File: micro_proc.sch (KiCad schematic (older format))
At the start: 1 part

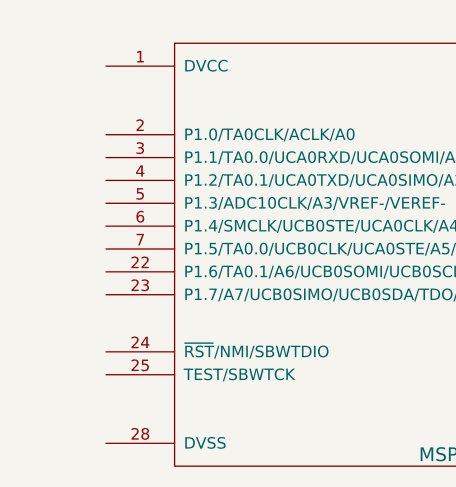
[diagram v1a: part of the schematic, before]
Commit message: added headlight sheet, led, dac
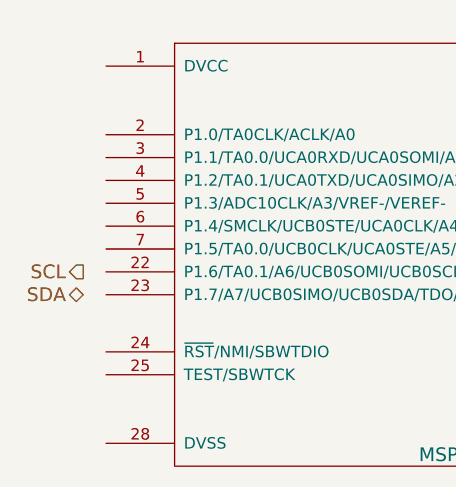
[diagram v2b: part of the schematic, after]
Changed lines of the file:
@@
 $Descr A4 11693 8268
 encoding utf-8
-Sheet 7 16
+Sheet 7 17
 Title ""
-Date "6 dec 2013"
+Date "7 dec 2013"
 Rev ""
 Comp ""
@@
 	1    0    0    -1
 $EndComp
+Text HLabel 4100 2950 0    60   BiDi ~ 0
+SDA
+Text HLabel 4100 2850 0    60   Output ~ 0
+SCL
 $EndSCHEMATC

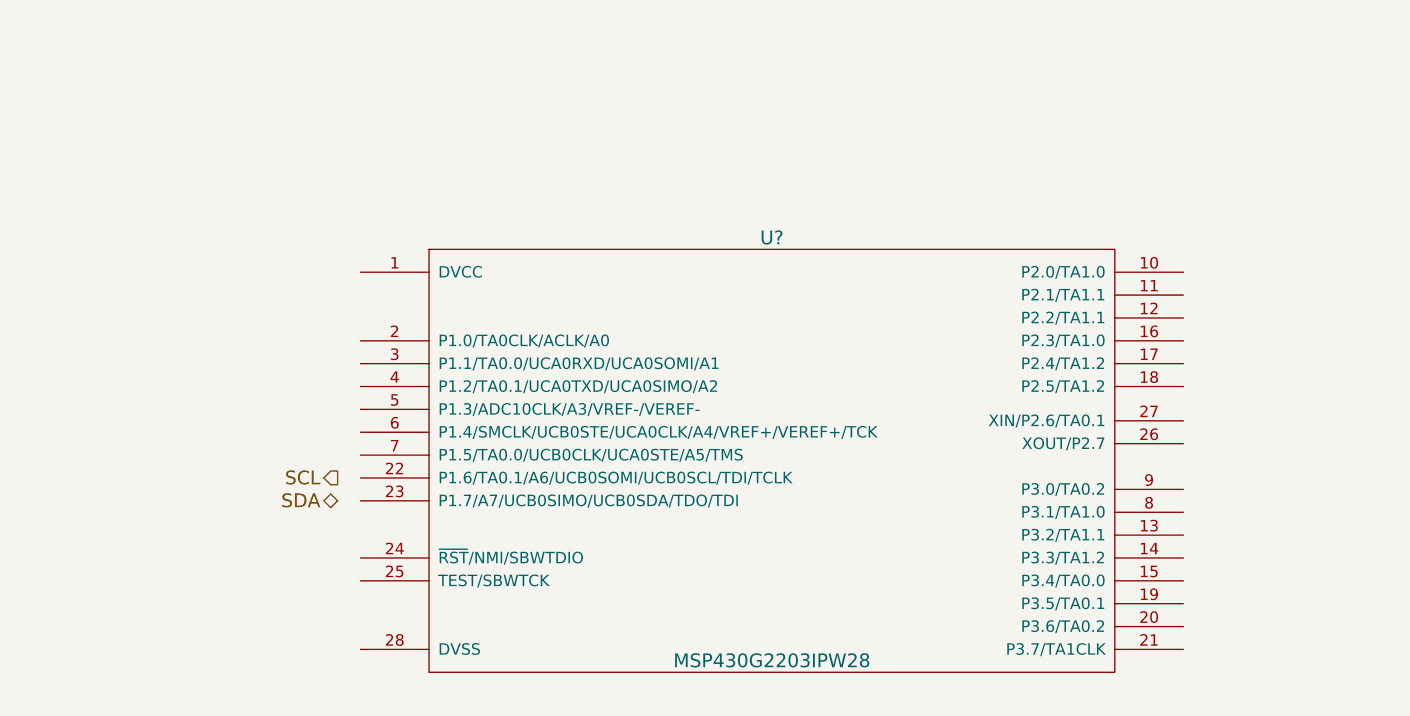
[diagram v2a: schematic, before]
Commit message: organized proc sheet I/O, organized I2C bus structure
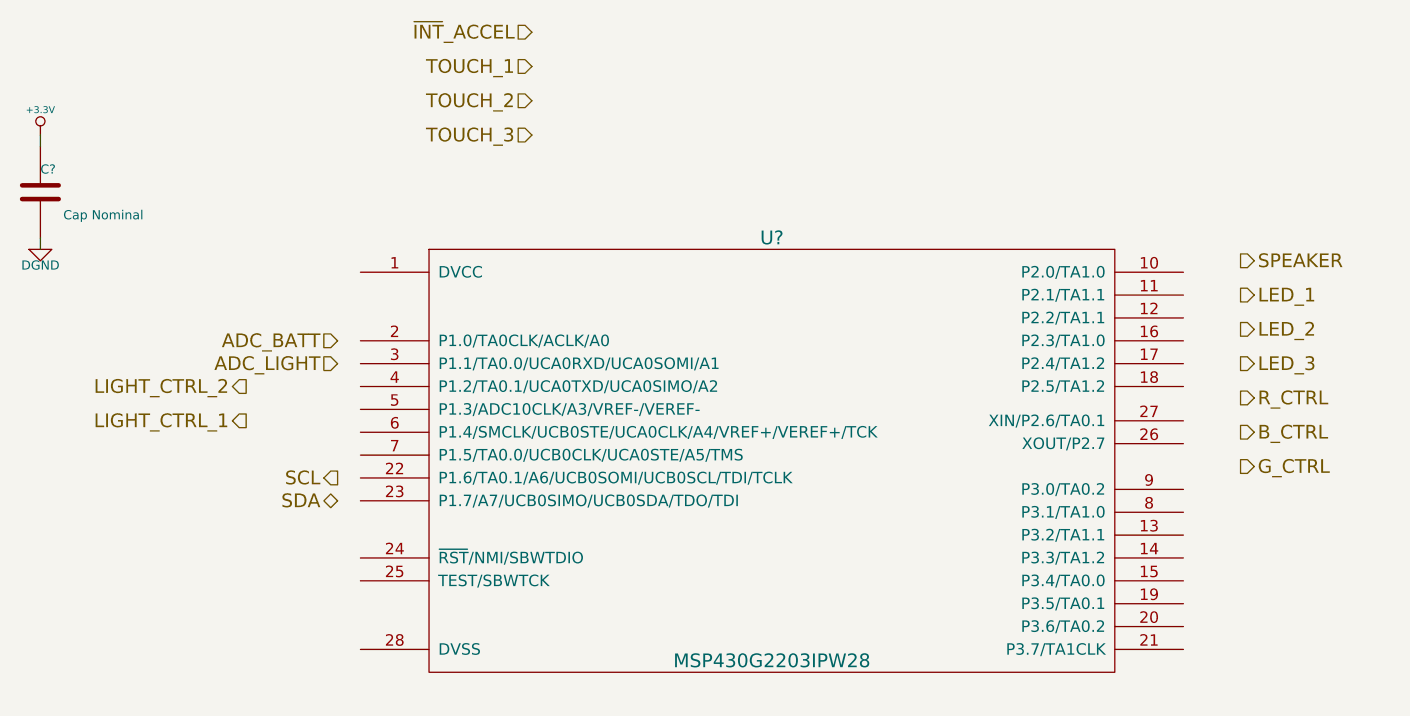
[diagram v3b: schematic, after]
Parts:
- added C?: Cap Nominal, ~, symbol C
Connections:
- new net +3.3V: C?.1
- new net DGND: C?.2
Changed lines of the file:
@@
 Text HLabel 4100 2850 0    60   Output ~ 0
 SCL
+$Comp
+L C C?
+U 1 1 52A38C98
+P 2800 1600
+F 0 "C?" H 2800 1700 40  0000 L CNN
+F 1 "Cap Nominal" H 2900 1500 40  0000 L CNN
+F 2 "~" H 2838 1450 30  0000 C CNN
+F 3 "~" H 2800 1600 60  0000 C CNN
+	1    2800 1600
+	1    0    0    -1
+$EndComp
+$Comp
+L +3.3V #PWR?
+U 1 1 52A38C9E
+P 2800 1350
+F 0 "#PWR?" H 2800 1310 30  0001 C CNN
+F 1 "+3.3V" H 2800 1460 30  0000 C CNN
+F 2 "" H 2800 1350 60  0000 C CNN
+F 3 "" H 2800 1350 60  0000 C CNN
+	1    2800 1350
+	1    0    0    -1
+$EndComp
+$Comp
+L DGND #PWR?
+U 1 1 52A38CA4
+P 2800 1850
+F 0 "#PWR?" H 2800 1850 40  0001 C CNN
+F 1 "DGND" H 2800 1780 40  0000 C CNN
+F 2 "" H 2800 1850 60  0000 C CNN
+F 3 "" H 2800 1850 60  0000 C CNN
+	1    2800 1850
+	1    0    0    -1
+$EndComp
+Wire Wire Line
+	2800 1350 2800 1400
+Wire Wire Line
+	2800 1800 2800 1850
+Text HLabel 4100 2250 0    60   Input ~ 0
+ADC_BATT
+Text HLabel 4100 2350 0    60   Input ~ 0
+ADC_LIGHT
+Text HLabel 4950 900  0    60   Input ~ 0
+~INT~_ACCEL
+Text HLabel 4950 1050 0    60   Input ~ 0
+TOUCH_1
+Text HLabel 4950 1200 0    60   Input ~ 0
+TOUCH_2
+Text HLabel 4950 1350 0    60   Input ~ 0
+TOUCH_3
+Text HLabel 8050 1900 2    60   Output ~ 0
+SPEAKER
+Text HLabel 8050 2050 2    60   Output ~ 0
+LED_1
+Text HLabel 8050 2200 2    60   Output ~ 0
+LED_2
+Text HLabel 8050 2350 2    60   Output ~ 0
+LED_3
+Text HLabel 8050 2500 2    60   Output ~ 0
+R_CTRL
+Text HLabel 8050 2650 2    60   Output ~ 0
+B_CTRL
+Text HLabel 8050 2800 2    60   Output ~ 0
+G_CTRL
+Text HLabel 3700 2600 0    60   Output ~ 0
+LIGHT_CTRL_1
+Text HLabel 3700 2450 0    60   Output ~ 0
+LIGHT_CTRL_2
 $EndSCHEMATC

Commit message: continued fleshing out proc
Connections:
- net +3.3V: now also U?.1 (DVCC)
- net ADC_BATT: now also U?.2 (P1.0/TA0CLK/ACLK/A0)
- net ADC_LIGHT: now also U?.5 (P1.3/ADC10CLK/A3/VREF-/VEREF-)
- net B_CTRL: now also U?.20 (P3.6/TA0.2)
- net DGND: now also U?.28 (DVSS)
- net G_CTRL: now also U?.19 (P3.5/TA0.1)
- net LED_1: now also U?.8 (P3.1/TA1.0)
- net LED_2: now also U?.13 (P3.2/TA1.1)
- net LED_3: now also U?.14 (P3.3/TA1.2)
- net LIGHT_CTRL_1: now also U?.27 (XIN/P2.6/TA0.1)
- net LIGHT_CTRL_2: now also U?.26 (XOUT/P2.7)
- net R_CTRL: now also U?.15 (P3.4/TA0.0)
- net SCL: now also U?.22 (P1.6/TA0.1/A6/UCB0SOMI/UCB0SCL/TDI/TCLK)
- net SDA: now also U?.23 (P1.7/A7/UCB0SIMO/UCB0SDA/TDO/TDI)
- net SPEAKER: now also U?.9 (P3.0/TA0.2)
- net TOUCH_1: now also U?.11 (P2.1/TA1.1)
- net TOUCH_2: now also U?.12 (P2.2/TA1.1)
- net TOUCH_3: now also U?.16 (P2.3/TA1.0)
- net ~INT~_ACCEL: now also U?.10 (P2.0/TA1.0)
- net UART_RX: now reaches U?.3 (P1.1/TA0.0/UCA0RXD/UCA0SOMI/A1)
- net UART_TX: now reaches U?.4 (P1.2/TA0.1/UCA0TXD/UCA0SIMO/A2)
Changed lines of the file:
@@
 Sheet 7 17
 Title ""
-Date "7 dec 2013"
+Date "8 dec 2013"
 Rev ""
 Comp ""
@@
 Text HLabel 4100 2250 0    60   Input ~ 0
 ADC_BATT
+Text HLabel 4100 2550 0    60   Input ~ 0
+ADC_LIGHT
+Text HLabel 7900 1950 2    60   Input ~ 0
+~INT~_ACCEL
+Text HLabel 7900 2050 2    60   Input ~ 0
+TOUCH_1
+Text HLabel 7900 2150 2    60   Input ~ 0
+TOUCH_2
+Text HLabel 7900 2250 2    60   Input ~ 0
+TOUCH_3
+Text HLabel 7900 2900 2    60   Output ~ 0
+SPEAKER
+Text HLabel 7900 3000 2    60   Output ~ 0
+LED_1
+Text HLabel 7900 3100 2    60   Output ~ 0
+LED_2
+Text HLabel 7900 3200 2    60   Output ~ 0
+LED_3
+Text HLabel 7900 3300 2    60   Output ~ 0
+R_CTRL
+Text HLabel 7900 3500 2    60   Output ~ 0
+B_CTRL
+Text HLabel 7900 3400 2    60   Output ~ 0
+G_CTRL
+Text HLabel 7900 2600 2    60   Output ~ 0
+LIGHT_CTRL_1
+Text HLabel 7900 2700 2    60   Output ~ 0
+LIGHT_CTRL_2
+Wire Wire Line
+	4100 2950 4200 2950
+Wire Wire Line
+	4100 2850 4200 2850
+$Comp
+L +3.3V #PWR?
+U 1 1 52A4573A
+P 4200 1850
+F 0 "#PWR?" H 4200 1810 30  0001 C CNN
+F 1 "+3.3V" H 4200 1960 30  0000 C CNN
+F 2 "" H 4200 1850 60  0000 C CNN
+F 3 "" H 4200 1850 60  0000 C CNN
+	1    4200 1850
+	1    0    0    -1
+$EndComp
+Wire Wire Line
+	4200 1850 4200 1950
+$Comp
+L DGND #PWR?
+U 1 1 52A45745
+P 4200 3700
+F 0 "#PWR?" H 4200 3700 40  0001 C CNN
+F 1 "DGND" H 4200 3630 40  0000 C CNN
+F 2 "" H 4200 3700 60  0000 C CNN
+F 3 "" H 4200 3700 60  0000 C CNN
+	1    4200 3700
+	1    0    0    -1
+$EndComp
+Wire Wire Line
+	4200 3700 4200 3600
+Wire Wire Line
+	4100 2250 4200 2250
+Wire Wire Line
+	4100 2550 4200 2550
+Wire Wire Line
+	7800 1950 7900 1950
+Wire Wire Line
+	7800 2050 7900 2050
+Wire Wire Line
+	7800 2150 7900 2150
+Wire Wire Line
+	7800 2250 7900 2250
+Wire Wire Line
+	7800 2600 7900 2600
+Wire Wire Line
+	7900 2700 7800 2700
+Wire Wire Line
+	7800 2900 7900 2900
+Wire Wire Line
+	7900 3000 7800 3000
+Wire Wire Line
+	7800 3100 7900 3100
+Wire Wire Line
+	7900 3200 7800 3200
+Wire Wire Line
+	7800 3300 7900 3300
+Wire Wire Line
+	7900 3400 7800 3400
+Wire Wire Line
+	7800 3500 7900 3500
 Text HLabel 4100 2350 0    60   Input ~ 0
-ADC_LIGHT
-Text HLabel 4950 900  0    60   Input ~ 0
-~INT~_ACCEL
-Text HLabel 4950 1050 0    60   Input ~ 0
-TOUCH_1
-Text HLabel 4950 1200 0    60   Input ~ 0
-TOUCH_2
-Text HLabel 4950 1350 0    60   Input ~ 0
-TOUCH_3
-Text HLabel 8050 1900 2    60   Output ~ 0
-SPEAKER
-Text HLabel 8050 2050 2    60   Output ~ 0
-LED_1
-Text HLabel 8050 2200 2    60   Output ~ 0
-LED_2
-Text HLabel 8050 2350 2    60   Output ~ 0
-LED_3
-Text HLabel 8050 2500 2    60   Output ~ 0
-R_CTRL
-Text HLabel 8050 2650 2    60   Output ~ 0
-B_CTRL
-Text HLabel 8050 2800 2    60   Output ~ 0
-G_CTRL
-Text HLabel 3700 2600 0    60   Output ~ 0
-LIGHT_CTRL_1
-Text HLabel 3700 2450 0    60   Output ~ 0
-LIGHT_CTRL_2
+UART_RX
+Text HLabel 4100 2450 0    60   Output ~ 0
+UART_TX
+Wire Wire Line
+	4100 2350 4200 2350
+Wire Wire Line
+	4200 2450 4100 2450
 $EndSCHEMATC

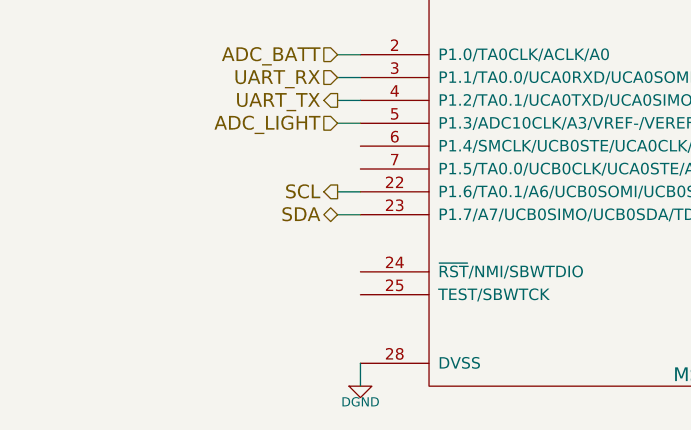
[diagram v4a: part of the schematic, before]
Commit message: general organization, fixed power reg sheet, added jtag
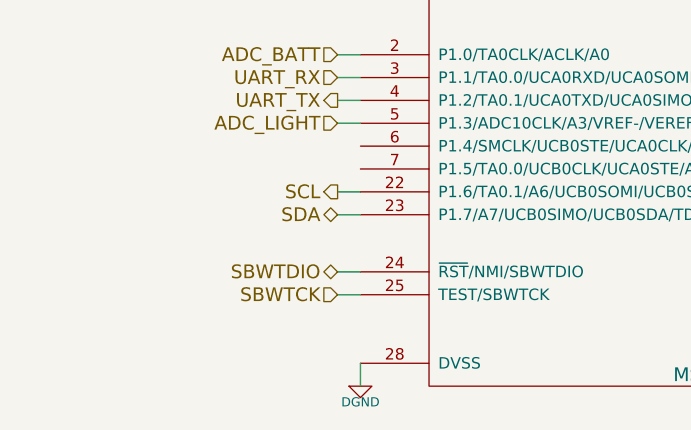
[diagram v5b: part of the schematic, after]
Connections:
- net SBWTDIO: now reaches U?.24 (~RST~/NMI/SBWTDIO)
- net SBWTCK: now reaches U?.25 (TEST/SBWTCK)
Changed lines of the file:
@@
 $Descr A4 11693 8268
 encoding utf-8
-Sheet 7 17
+Sheet 6 18
 Title ""
 Date "8 dec 2013"
@@
 Wire Wire Line
 	4200 2450 4100 2450
+Text HLabel 4100 3300 0    60   Input ~ 0
+SBWTCK
+Text HLabel 4100 3200 0    60   BiDi ~ 0
+SBWTDIO
+Wire Wire Line
+	4100 3200 4200 3200
+Wire Wire Line
+	4100 3300 4200 3300
 $EndSCHEMATC

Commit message: Minor fixes, labels, etc
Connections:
- net SPEAKER: now also U?.17 (P2.4/TA1.2); no longer U?.9 (P3.0/TA0.2)
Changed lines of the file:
@@
 Sheet 6 18
 Title ""
-Date "10 dec 2013"
+Date "11 dec 2013"
 Rev ""
 Comp ""
@@
 Text HLabel 7900 2250 2    60   Input ~ 0
 TOUCH_3
-Text HLabel 7900 2900 2    60   Output ~ 0
+Text HLabel 7900 2350 2    60   Output ~ 0
 SPEAKER
 Text HLabel 7900 3000 2    60   Output ~ 0
@@
 	7900 2700 7800 2700
 Wire Wire Line
-	7800 2900 7900 2900
+	7800 2350 7900 2350
 Wire Wire Line
 	7900 3000 7800 3000
